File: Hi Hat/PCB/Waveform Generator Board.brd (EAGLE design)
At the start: 100 x 50 mm, 94 parts, among them IC1 LM741P, Q1 2N2222A, Q10 2N3904, Q11 2N3904, Q12 2N3904, Q2 2N2222A, Q3 2N2222A, Q4 2N2222A, Q5 2N2222A, Q6 2N2222A, Q7 2N2222A, Q8 2N2222A, Q9 2N3904

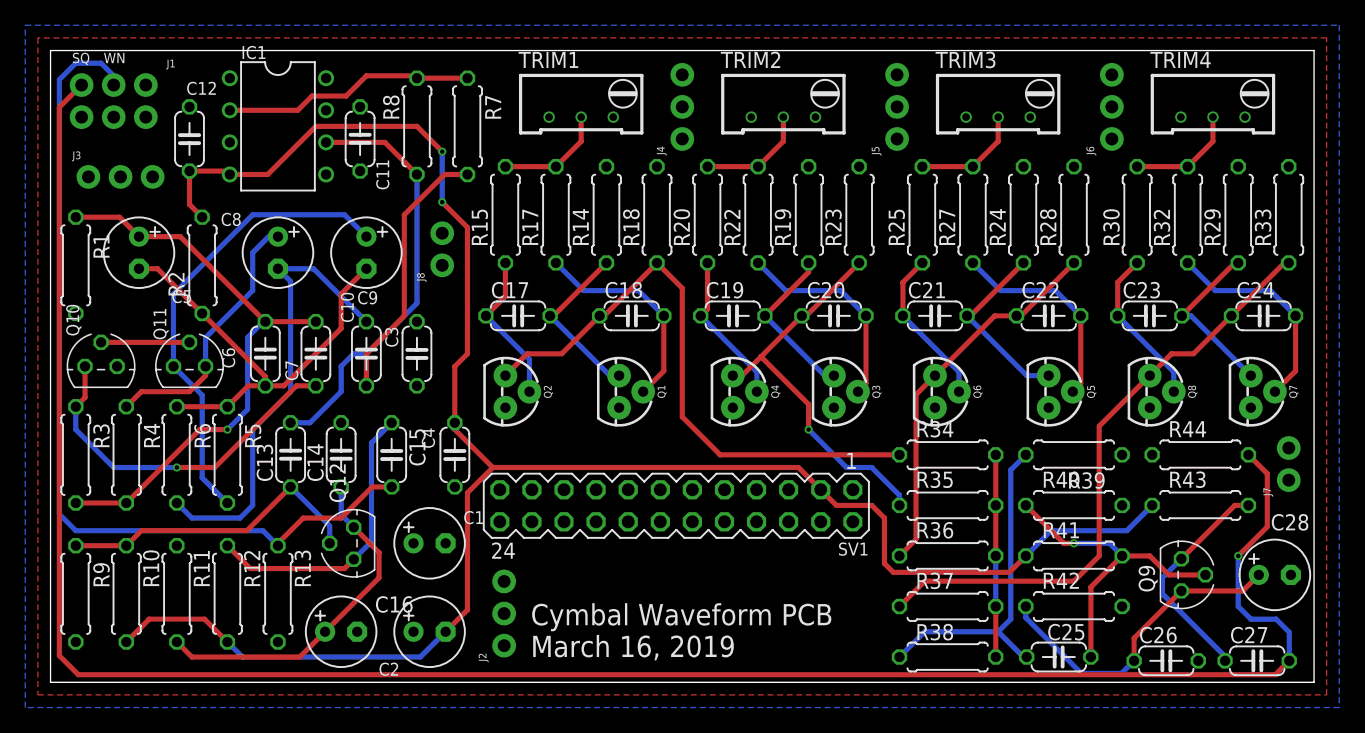
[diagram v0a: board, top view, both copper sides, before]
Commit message: Worked on Hi-hat and waveform generator board
Changed trimpots to the proper part. Added test points to the waveform generator board and fixed silkscreen, ran DRC.
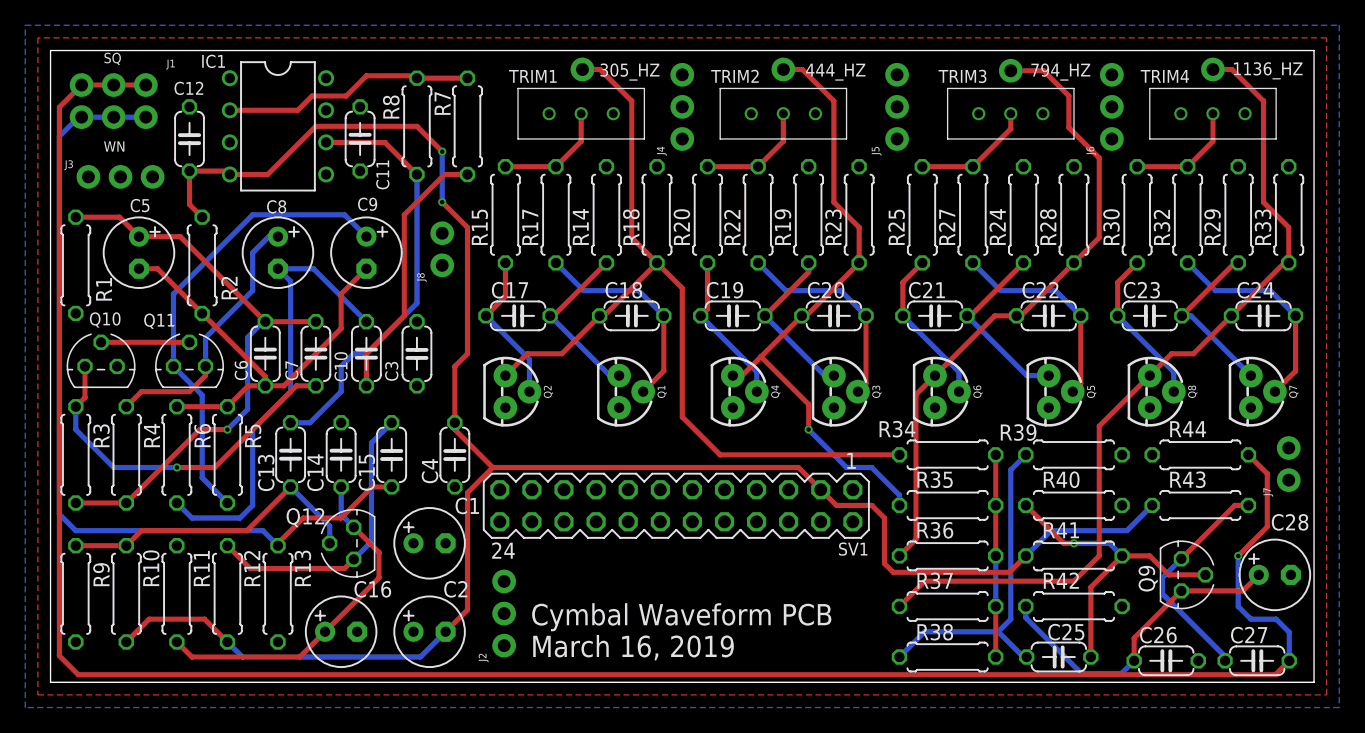
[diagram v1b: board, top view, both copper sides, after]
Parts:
- added 1136_HZ, 305_HZ, 444_HZ, 794_HZ: (no value), SparkFun-Connectors:1X01NS_KIT
- TRIM1, TRIM2, TRIM3, TRIM4: device rcl:RTRIM64W -> Capstone:10K_TRIM
- moved TRIM1 5.83 mm to (37.0, 43.0), turned to 0 degrees
- moved TRIM2 5.83 mm to (53.0, 43.0), turned to 0 degrees
- moved TRIM4 5.83 mm to (87.0, 43.0), turned to 0 degrees
- moved TRIM3 5.00 mm to (71.0, 43.0), turned to 0 degrees
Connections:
- net +12V: now also TRIM1.P$3, TRIM2.P$3, TRIM3.P$3, TRIM4.P$3; no longer TRIM1.3, TRIM2.3, TRIM3.3, TRIM4.3
- net N$15: now also TRIM1.P$2; no longer TRIM1.2
- net N$29: now also TRIM2.P$2; no longer TRIM2.2
- net N$54: now also TRIM3.P$2; no longer TRIM3.2
- net N$59: now also TRIM4.P$2; no longer TRIM4.2
- net OSC1: now also 305_HZ.1
- net OSC2: now also 444_HZ.1
- net OSC3: now also 794_HZ.1
- net OSC4: now also 1136_HZ.1
- net SQUARE_WAVE_BUFFERED: now also J1.4, J1.6
- net WHITE_NOISE_BUFFERED: now also J1.1, J1.3, J1.5; no longer J1.4
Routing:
- net OSC3: track 30.1 -> 50.6 mm
- net OSC4: track 48.1 -> 66.8 mm
- net OSC2: track 31.2 -> 49.9 mm
- net OSC1: track 47.1 -> 65.7 mm
- net SQUARE_WAVE_BUFFERED: track 165.0 -> 170.1 mm
- net WHITE_NOISE_BUFFERED: track 69.8 -> 66.7 mm
- net N$54: track 8.75 -> 9.43 mm

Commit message: Generated Gerbers
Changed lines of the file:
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@@
 <?xml version="1.0" encoding="utf-8"?>
 <!DOCTYPE eagle SYSTEM "eagle.dtd">
-<eagle version="9.3.0">
+<eagle version="9.2.2">
 <drawing>
 <settings>
@@
 <wire x1="100" y1="50" x2="0" y2="50" width="0" layer="20"/>
 <wire x1="0" y1="50" x2="0" y2="0" width="0" layer="20"/>
-<text x="64" y="20" size="1.016" layer="26" rot="MR270">+12V</text>
-<text x="61.5" y="20" size="1.016" layer="26" rot="MR270">-12V</text>
+<text x="63" y="20" size="1.016" layer="25" rot="R270">+12V</text>
+<text x="60.5" y="20" size="1.016" layer="25" rot="R270">-12V</text>
 <text x="38" y="2" size="1.6764" layer="21">Cymbal Waveform PCB
 March 16, 2019</text>
